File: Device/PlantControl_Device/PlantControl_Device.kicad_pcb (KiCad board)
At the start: 2 copper layers, 14 parts, among them J2 Power, U1 NRF24L01_Breakout, U2 PIC18F15Q41-I/SS, U3 AHT20, U4 BH1750FVI-TR, U5 NCP1117-3.3Vout-20Vin

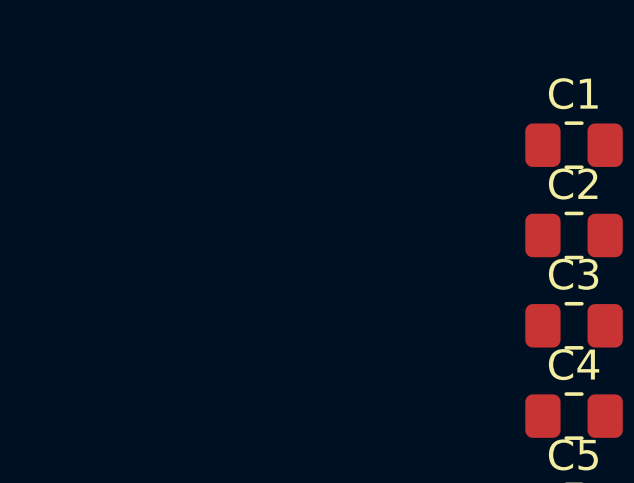
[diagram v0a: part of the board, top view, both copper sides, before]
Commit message: Added PowerGood LEDs for 9V and 3.3V
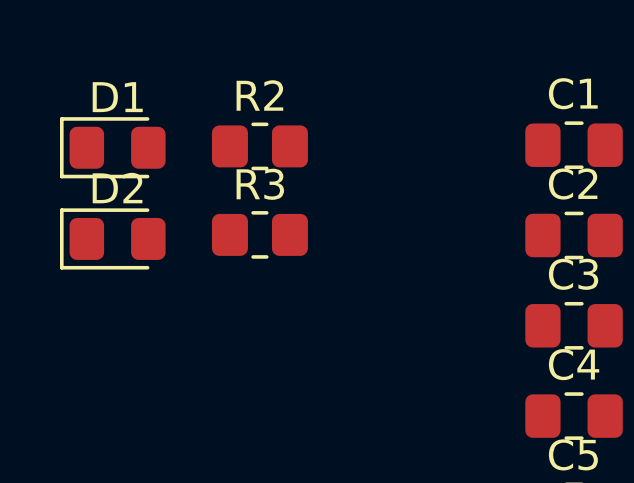
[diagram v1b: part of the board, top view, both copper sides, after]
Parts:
- added D1: LED_Blue, LED_SMD:LED_0805_2012Metric_Pad1.15x1.40mm_HandSolder, F.Cu at (23.3, 27.6)
- added D2: LED_Yellow, LED_SMD:LED_0805_2012Metric_Pad1.15x1.40mm_HandSolder, F.Cu at (23.3, 30.6)
- added R2: 290R, Resistor_SMD:R_0805_2012Metric_Pad1.20x1.40mm_HandSolder, F.Cu at (28.0, 27.6)
- added R3: 60R, Resistor_SMD:R_0805_2012Metric_Pad1.20x1.40mm_HandSolder, F.Cu at (28.0, 30.5)

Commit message: First layout
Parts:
- removed C7: 0.1uF, Capacitor_SMD:C_0805_2012Metric_Pad1.18x1.45mm_HandSolder
- added C8: 10uF, Capacitor_THT:C_Disc_D4.3mm_W1.9mm_P5.00mm, F.Cu at (91.0, 81.0)
- added D3: LED_RGBA, cr_Library:cr_RGB_LED, B.Cu at (100.2, 69.0)
- added D4: LED_RGBA, cr_Library:cr_RGB_LED, B.Cu at (73.3, 84.3)
- added D5: LED_RGBA, cr_Library:cr_RGB_LED, B.Cu at (86.3, 116.4)
- added D6: LED_RGBA, cr_Library:cr_RGB_LED, B.Cu at (115.4, 114.8)
- added D7: LED_RGBA, cr_Library:cr_RGB_LED, B.Cu at (126.8, 84.6)
- added J1: ADC1, Connector_PinHeader_2.00mm:PinHeader_1x03_P2.00mm_Vertical, F.Cu at (112.5, 77.8)
- added J3: ADC2, Connector_PinHeader_2.00mm:PinHeader_1x03_P2.00mm_Vertical, F.Cu at (114.5, 74.7)
- added J5: Conn_ARM_SWD_TagConnect_TC2030-NL, Connector:Tag-Connect_TC2030-IDC-NL_2x03_P1.27mm_Vertical, B.Cu at (97.6, 79.7)
- added R10: R, Resistor_THT:R_Axial_DIN0207_L6.3mm_D2.5mm_P7.62mm_Horizontal, B.Cu at (66.7, 86.3)
- added R11: R, Resistor_THT:R_Axial_DIN0207_L6.3mm_D2.5mm_P7.62mm_Horizontal, B.Cu at (81.7, 128.8)
- added R12: R, Resistor_THT:R_Axial_DIN0207_L6.3mm_D2.5mm_P7.62mm_Horizontal, B.Cu at (127.3, 120.4)
- added R13: R, Resistor_THT:R_Axial_DIN0207_L6.3mm_D2.5mm_P7.62mm_Horizontal, B.Cu at (75.9, 129.5)
- added R14: R, Resistor_THT:R_Axial_DIN0207_L6.3mm_D2.5mm_P7.62mm_Horizontal, B.Cu at (127.5, 126.3)
- added R15: R, Resistor_THT:R_Axial_DIN0207_L6.3mm_D2.5mm_P7.62mm_Horizontal, B.Cu at (73.2, 124.2)
- added R16: R, Resistor_THT:R_Axial_DIN0207_L6.3mm_D2.5mm_P7.62mm_Horizontal, B.Cu at (122.1, 128.5)
- added R17: R, Resistor_THT:R_Axial_DIN0207_L6.3mm_D2.5mm_P7.62mm_Horizontal, B.Cu at (131.5, 86.9)
- added R18: R, Resistor_THT:R_Axial_DIN0207_L6.3mm_D2.5mm_P7.62mm_Horizontal, B.Cu at (133.2, 81.4)
- added R19: R, Resistor_THT:R_Axial_DIN0207_L6.3mm_D2.5mm_P7.62mm_Horizontal, B.Cu at (128.6, 77.7)
- added R20: R, Resistor_SMD:R_0805_2012Metric_Pad1.20x1.40mm_HandSolder, F.Cu at (85.7, 76.9)
- added R21: R, Resistor_SMD:R_0805_2012Metric_Pad1.20x1.40mm_HandSolder, F.Cu at (89.2, 74.9)
- added R4: 1kR, Resistor_SMD:R_0805_2012Metric_Pad1.20x1.40mm_HandSolder, F.Cu at (110.9, 108.9)
- added R5: R, Resistor_THT:R_Axial_DIN0207_L6.3mm_D2.5mm_P7.62mm_Horizontal, B.Cu at (104.6, 66.1)
- added R6: R, Resistor_THT:R_Axial_DIN0207_L6.3mm_D2.5mm_P7.62mm_Horizontal, B.Cu at (100.5, 61.9)
- added R7: R, Resistor_THT:R_Axial_DIN0207_L6.3mm_D2.5mm_P7.62mm_Horizontal, B.Cu at (95.2, 64.5)
- added R8: R, Resistor_THT:R_Axial_DIN0207_L6.3mm_D2.5mm_P7.62mm_Horizontal, B.Cu at (73.1, 79.1)
- added R9: R, Resistor_THT:R_Axial_DIN0207_L6.3mm_D2.5mm_P7.62mm_Horizontal, B.Cu at (67.4, 80.3)
- C1, U3: moved to B.Cu
- moved D1 122.7 mm to (124.9, 96.3), turned to -10 degrees
- moved D2 122.1 mm to (124.5, 98.8), turned to -10 degrees
- moved R2 115.5 mm to (121.2, 95.7), turned to 170 degrees
- moved R3 114.9 mm to (120.8, 98.2), turned to 170 degrees
- moved C5 111.2 mm to (130.4, 102.1), turned to -10 degrees
- moved J2 110.7 mm to (130.0, 104.6), turned to -10 degrees
- moved U5 107.6 mm to (123.5, 104.5), turned to 170 degrees
- moved C4 105.3 mm to (109.5, 114.3), turned to 90 degrees
- moved C6 99.9 mm to (118.4, 102.5), turned to 80 degrees
- moved C1 82.0 mm to (70.8, 102.9), turned to -120 degrees
- moved U1 80.6 mm to (106.0, 110.7), turned to -90 degrees
- moved C3 63.1 mm to (88.5, 72.0), turned to -60 degrees
- moved C2 62.7 mm to (83.2, 74.5), turned to -60 degrees
- moved U3 60.7 mm to (73.7, 105.8), turned to -30 degrees
- moved R1 54.5 mm to (82.6, 77.2), turned to 120 degrees
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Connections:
- U1 pad 3: unconnected-(U1-CE-Pad3) -> NRF_CE
- U1 pad 4: unconnected-(U1-~{CSN}-Pad4) -> SPI_nCS
- U1 pad 5: unconnected-(U1-SCK-Pad5) -> SPI_SCK
- U1 pad 6: unconnected-(U1-MOSI-Pad6) -> SPI_MOSI
- U1 pad 7: unconnected-(U1-MISO-Pad7) -> SPI_MISO
- U1 pad 8: unconnected-(U1-IRQ-Pad8) -> NRF_IRQ
- U2 pad 13: unconnected-(U2-RB4-Pad13) -> RGB2_B
- U2 pad 14: unconnected-(U2-RC2-Pad14) -> RGB2_G
- U2 pad 15: unconnected-(U2-RC1-Pad15) -> RGB2_R
- U2 pad 18: unconnected-(U2-RA1/ICSPCLK-Pad18) -> SWCLK
- U2 pad 19: unconnected-(U2-RA0/ICSPDAT-Pad19) -> SWDIO
- U2 pad 2: unconnected-(U2-RA5-Pad2) -> I2C_SCL
- U2 pad 3: unconnected-(U2-RA4-Pad3) -> I2C_SDA
- U2 pad 4: unconnected-(U2-*MCLR/VPP/RA3-Pad4) -> nRST
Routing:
- net +3.3V: track 0.00 -> 35.7 mm, vias 0 -> 1
- net +9V: track 0.00 -> 12.8 mm, vias 0 -> 1
- net Net-(D2-K): track 0.00 -> 1.76 mm
- net Net-(D1-K): track 0.00 -> 1.73 mm
- net SWDIO: vias 0 -> 1
- net SWCLK: vias 0 -> 1
- net I2C_SDA: vias 0 -> 1
- net I2C_SCL: vias 0 -> 1
- net GND: vias 0 -> 78
- added copper zone on B.Cu, net GND
- added copper zone on F.Cu, net GND
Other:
- board outline added: 80 x 80 mm
